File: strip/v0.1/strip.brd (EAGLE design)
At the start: 67 x 11.5 mm, 95 parts, among them IC1 LP2992, IC2 ADP3110A-SO8, IC4 OPA335, IC5 ADP3110A-SO8, IC6 ADP3110A-SO8, IC7 STM32F050CX, Q1 IRF7828, Q2 IRF7828, Q3 IRF7828, Q4 IRF7828, Q5 IRF7828, Q6 IRF7828

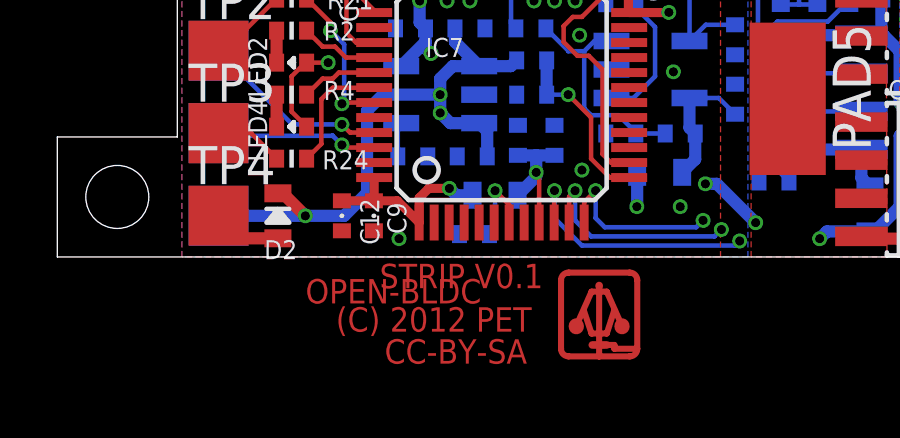
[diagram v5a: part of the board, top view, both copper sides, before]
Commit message: Added silkscreen obldc logo. Put the logo and text on the pcb.
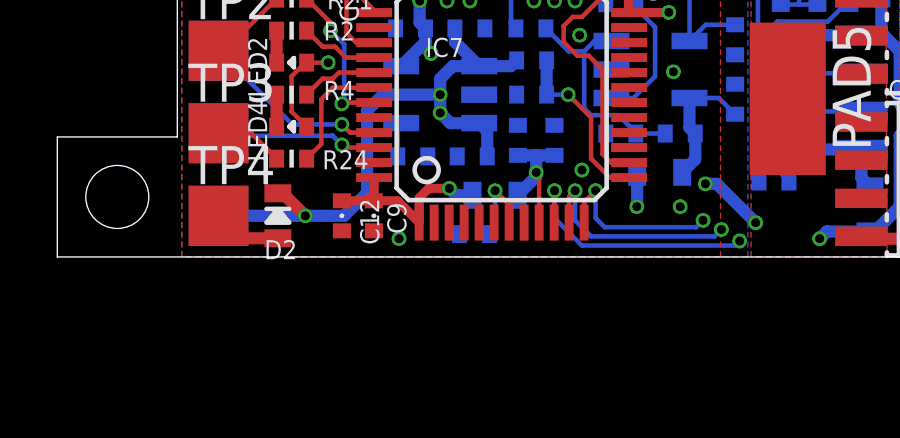
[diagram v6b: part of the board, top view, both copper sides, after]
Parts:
- D2: device pel_dipol_comp:0603-LED -> pel_dipol_comp:0603-DIO
- U$1: device open-bldc:LOGO -> open-bldc:LOGO_SILK_SMALL
- moved U$1 42.9 mm to (56.4, 4.22), flipped to the bottom
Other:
- board text added: "C12PET"
- board text added: "CCBYSA"
- board text added: "OBLDC"
- board text added: "STRIP"
- board text removed: "(C) 2012 PET"
- board text removed: "CC-BY-SA"
- board text removed: "OPEN-BLDC"
- board text removed: "STRIP V0.1"
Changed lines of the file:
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@@
 <layers>
 <layer number="1" name="Top" color="4" fill="1" visible="yes" active="yes"/>
-<layer number="2" name="Route2" color="1" fill="3" visible="yes" active="yes"/>
+<layer number="2" name="Route2" color="1" fill="3" visible="no" active="yes"/>
 <layer number="3" name="Route3" color="4" fill="3" visible="no" active="no"/>
 <layer number="4" name="Route4" color="1" fill="4" visible="no" active="no"/>
@@
 <layer number="13" name="Route13" color="4" fill="5" visible="no" active="no"/>
 <layer number="14" name="Route14" color="1" fill="6" visible="no" active="no"/>
-<layer number="15" name="Route15" color="4" fill="6" visible="yes" active="yes"/>
+<layer number="15" name="Route15" color="4" fill="6" visible="no" active="yes"/>
 <layer number="16" name="Bottom" color="1" fill="1" visible="yes" active="yes"/>
 <layer number="17" name="Pads" color="2" fill="1" visible="yes" active="yes"/>
@@
 <wire x1="0" y1="4" x2="-4" y2="4" width="0" layer="20"/>
 <wire x1="-4" y1="4" x2="-4" y2="0" width="0" layer="20"/>
-<text x="10.1346" y="-0.7366" size="0.8128" layer="1" font="vector" ratio="19" rot="R180">OPEN-BLDC</text>
-<text x="12.192" y="-0.2286" size="0.8128" layer="1" font="vector" ratio="19" rot="R180">STRIP V0.1</text>
-<text x="10.1346" y="-0.7366" size="0.8128" layer="29" font="vector" ratio="19" rot="R180">OPEN-BLDC</text>
-<text x="12.192" y="-0.2286" size="0.8128" layer="29" font="vector" ratio="19" rot="R180">STRIP V0.1</text>
-<text x="11.811" y="-1.6764" size="0.8128" layer="1" font="vector" ratio="19" rot="R180">(C) 2012 PET</text>
-<text x="11.811" y="-1.6764" size="0.8128" layer="29" font="vector" ratio="19" rot="R180">(C) 2012 PET</text>
-<text x="11.6586" y="-2.7432" size="0.8128" layer="1" font="vector" ratio="19" rot="R180">CC-BY-SA</text>
-<text x="11.6586" y="-2.7432" size="0.8128" layer="29" font="vector" ratio="19" rot="R180">CC-BY-SA</text>
+<text x="57.8104" y="4.191" size="0.8128" layer="22" font="vector" ratio="19" rot="MR90" align="bottom-center">OBLDC</text>
+<text x="54.102" y="4.2672" size="0.8128" layer="22" font="vector" ratio="19" rot="MR90" align="bottom-center">STRIP</text>
+<text x="56.3118" y="1.0668" size="0.8128" layer="22" font="vector" ratio="19" rot="MR180" align="bottom-center">C12PET</text>
+<text x="56.3118" y="2.1336" size="0.8128" layer="22" font="vector" ratio="19" rot="MR180" align="bottom-center">CCBYSA</text>
 <rectangle x1="23.6093" y1="21.0947" x2="23.8633" y2="21.1201" layer="42"/>
 <rectangle x1="19.8247" y1="20.9931" x2="20.0787" y2="21.0185" layer="42"/>
@@
 <attribute name="VALUE" x="11.7798" y="1.0278" size="1.27" layer="28" rot="MR0"/>
 </element>
-<element name="D2" library="pel_dipol_comp" package="0603-LED" value="CDBU0130" x="3.3528" y="1.3716" smashed="yes" rot="R270">
+<element name="D2" library="pel_dipol_comp" package="0603-DIO" value="CDBU0130" x="3.3528" y="1.3716" smashed="yes" rot="R270">
 <attribute name="NAME" x="2.8956" y="-0.0762" size="0.635" layer="25" font="vector" ratio="16"/>
 <attribute name="VALUE" x="1.4478" y="2.0066" size="1.27" layer="27" rot="R270"/>
@@
 <attribute name="VALUE" x="4.445" y="7.3152" size="1.27" layer="27" rot="R180"/>
 </element>
-<element name="U$1" library="open-bldc" package="LOGO" value="LOGO" x="14.0462" y="-2.032" smashed="yes"/>
+<element name="U$1" library="open-bldc" package="LOGO_SILK_SMALL" value="LOGO" x="56.4388" y="4.2164" smashed="yes" rot="MR0"/>
 <element name="LED2" library="pel_dipol_comp" package="0402-LED" value="GREEN" x="3.81" y="6.477" smashed="yes">
 <attribute name="NAME" x="2.9972" y="5.3086" size="0.635" layer="25" font="vector" ratio="16" rot="R90"/>

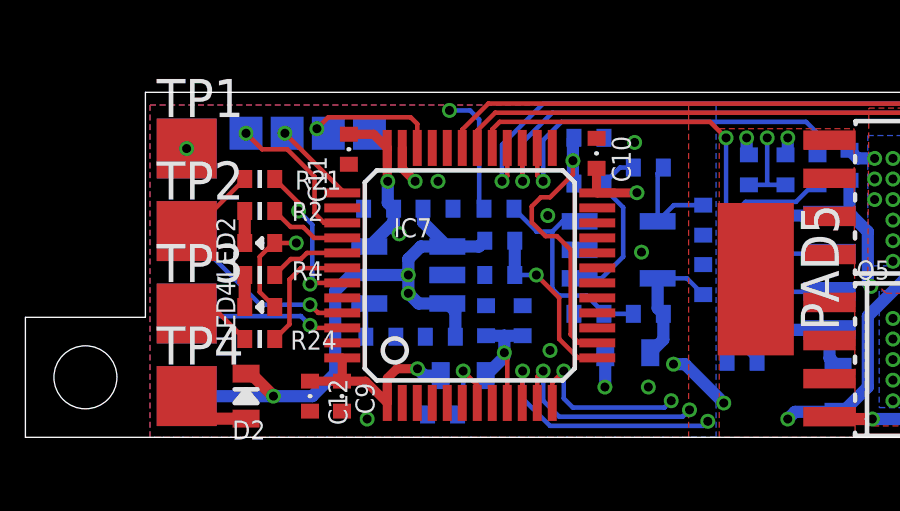
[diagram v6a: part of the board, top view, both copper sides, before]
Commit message: Corrected size of the 4.7uF capacitor for the STM32.
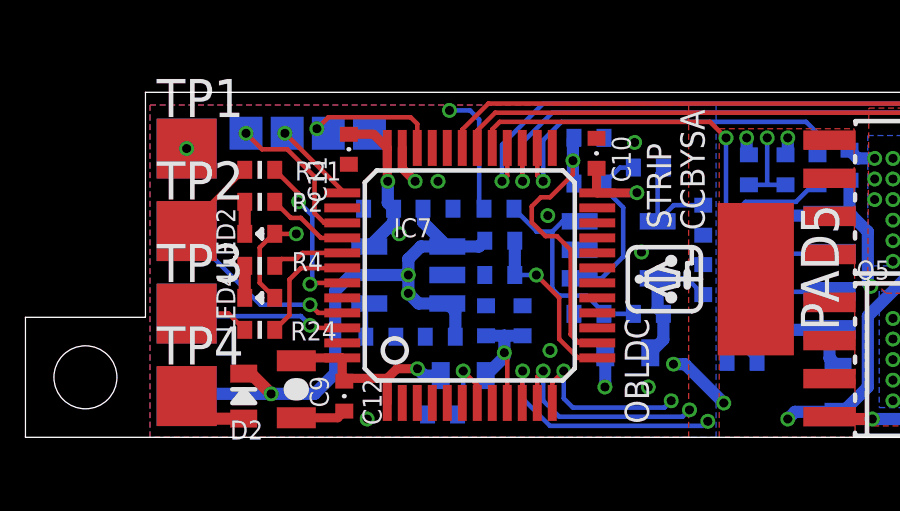
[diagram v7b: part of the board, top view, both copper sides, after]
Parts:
- added U$2: LOGO, open-bldc:LOGO_SILK_SMALL
- C9: device pel_dipol_comp:0402-CAP -> pel_dipol_comp:0805-CAP
- moved C9 1.54 mm to (5.03, 1.60)
- moved C12 1.14 mm to (6.63, 1.37)
- moved LED4 0.30 mm to (3.81, 4.65)
- moved R2 0.30 mm to (3.81, 7.85)
- moved R21 0.30 mm to (3.81, 8.92)
- moved R4 0.30 mm to (3.81, 5.71)
- moved R24 0.30 mm to (3.81, 3.58)
- moved LED2 0.30 mm to (3.81, 6.78)
- moved D2 0.08 mm to (3.28, 1.37)
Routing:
- net GND: track 45.9 -> 47.6 mm
